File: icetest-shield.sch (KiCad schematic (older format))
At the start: 7 parts

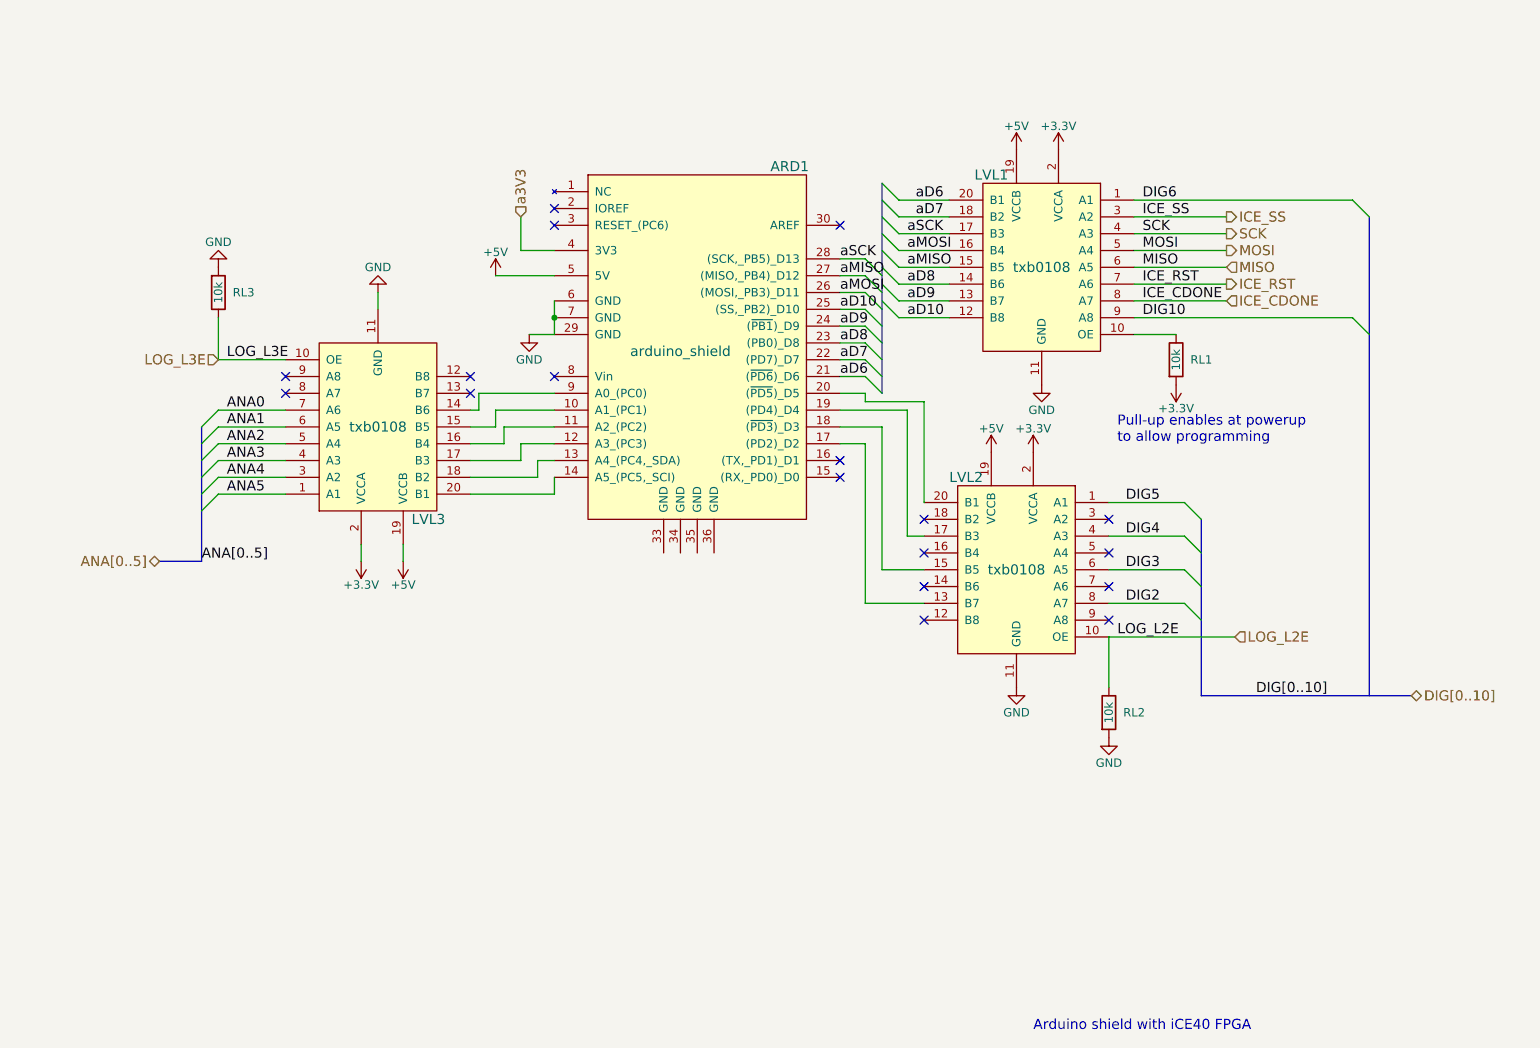
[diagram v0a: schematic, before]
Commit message: add SPI test points and verify footprints
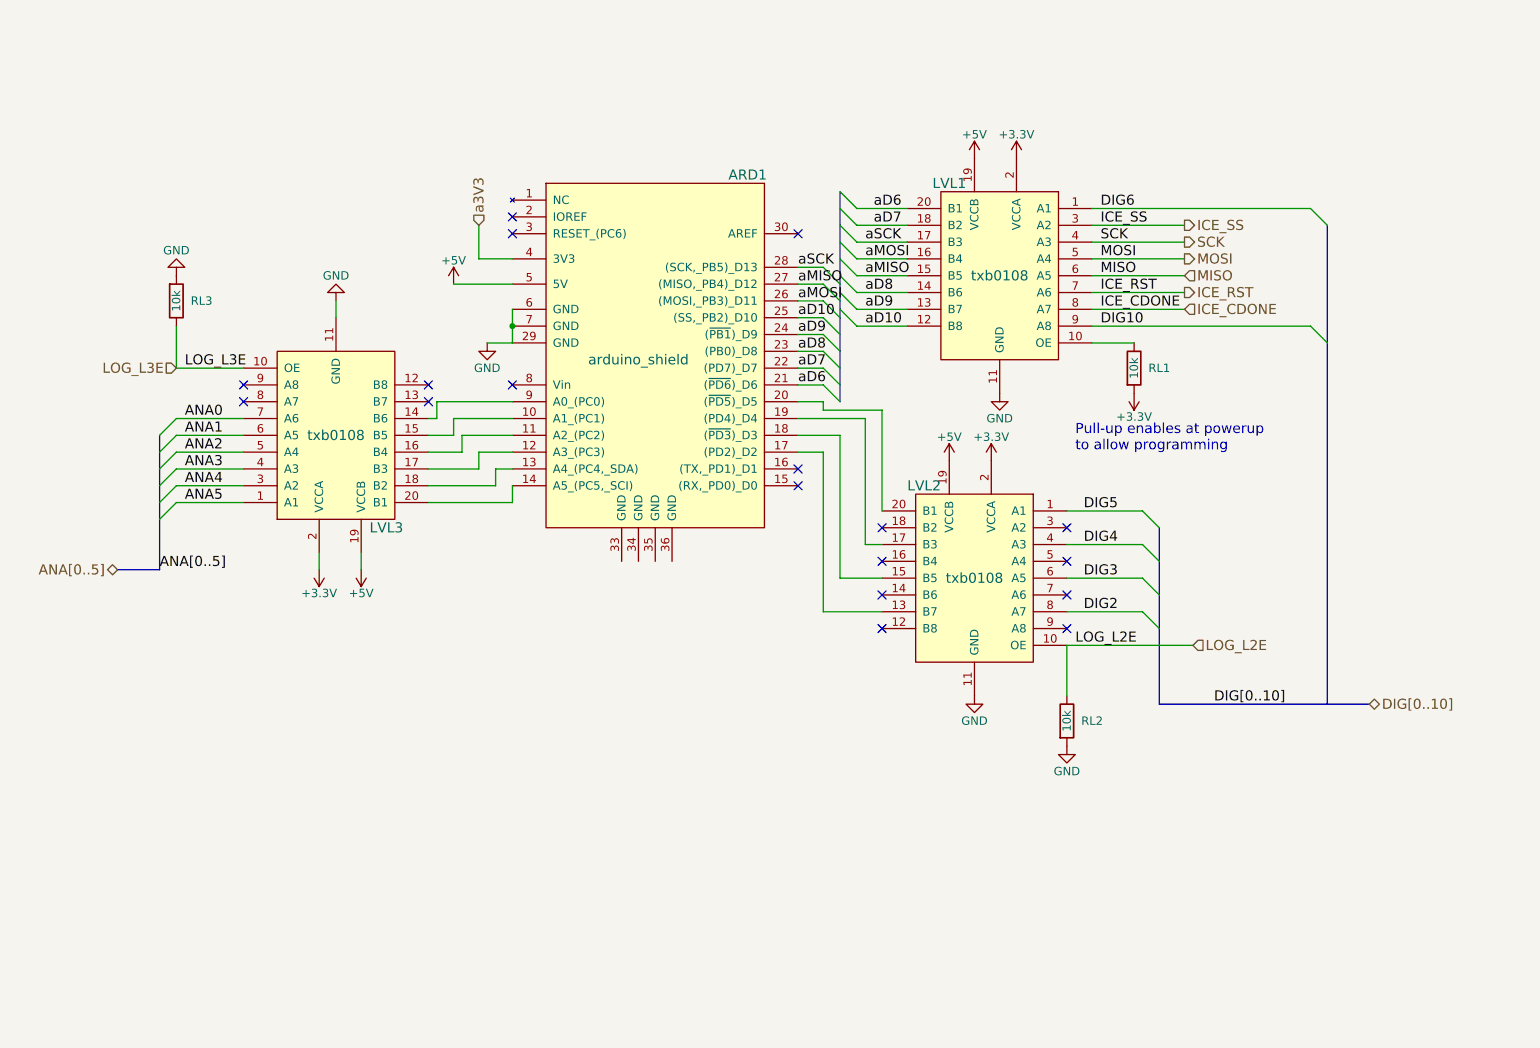
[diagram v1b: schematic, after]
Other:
- note removed: "Arduino shield with iCE40 FPGA"
- moved on the sheet: ARD1, LVL1, LVL2, LVL3, RL1, RL2, RL3

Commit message: route it
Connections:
- net GND: now also ARD1.33 (GND), ARD1.34 (GND), ARD1.35 (GND), ARD1.36 (GND)
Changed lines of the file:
@@
 	-1   0    0    1
 $EndComp
-Text HLabel 4050 2700 1    60   Input ~ 0
+Text HLabel 4050 2700 1    60   Output ~ 0
 a3V3
 NoConn ~ 5950 4150
@@
 Text HLabel 2250 3550 0    60   Input ~ 0
 LOG_L3E
+$Comp
+L GND #PWR?
+U 1 1 5793C5E6
+P 5100 4700
+F 0 "#PWR?" H 5100 4450 50  0001 C CNN
+F 1 "GND" H 5100 4550 50  0000 C CNN
+F 2 "" H 5100 4700 50  0000 C CNN
+F 3 "" H 5100 4700 50  0000 C CNN
+	1    5100 4700
+	-1   0    0    -1
+$EndComp
+Wire Wire Line
+	4900 4700 5200 4700
+Connection ~ 5100 4700
+Connection ~ 5000 4700
 $EndSCHEMATC

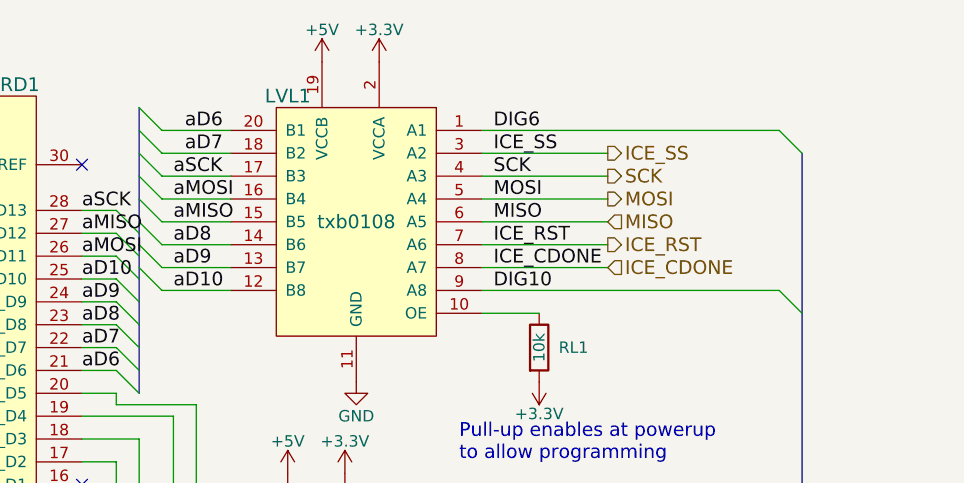
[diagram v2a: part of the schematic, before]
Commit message: fix ard symbol and route
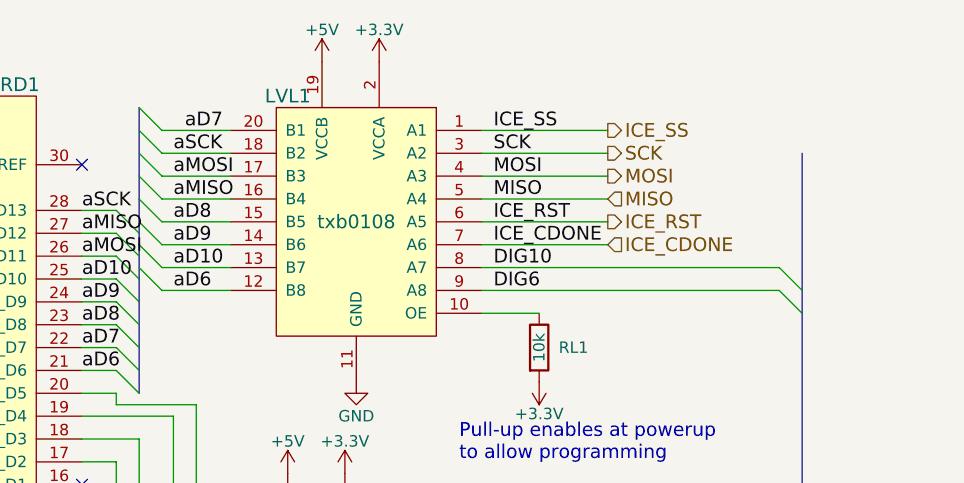
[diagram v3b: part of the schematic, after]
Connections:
- net DIG10: now also LVL1.8 (A7); no longer LVL1.9 (A8)
- net DIG6: now also LVL1.9 (A8); no longer LVL1.1 (A1)
- net ICE_CDONE: now also LVL1.7 (A6); no longer LVL1.8 (A7)
- net ICE_RST: now also LVL1.6 (A5); no longer LVL1.7 (A6)
- net ICE_SS: now also LVL1.1 (A1); no longer LVL1.3 (A2)
- net MISO: now also LVL1.5 (A4); no longer LVL1.6 (A5)
- net MOSI: now also LVL1.4 (A3); no longer LVL1.5 (A4)
- net SCK: now also LVL1.3 (A2); no longer LVL1.4 (A3)
- net aD10: now also LVL1.13 (B7); no longer LVL1.12 (B8)
- net aD6: now also LVL1.12 (B8); no longer LVL1.20 (B1)
- net aD7: now also LVL1.20 (B1); no longer LVL1.18 (B2)
- net aD8: now also LVL1.15 (B5); no longer LVL1.14 (B6)
- net aD9: now also LVL1.14 (B6); no longer LVL1.13 (B7)
- net aMISO: now also LVL1.16 (B4); no longer LVL1.15 (B5)
- net aMOSI: now also LVL1.17 (B3); no longer LVL1.16 (B4)
- net aSCK: now also LVL1.18 (B2); no longer LVL1.17 (B3)
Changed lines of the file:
@@
 $EndComp
+Entry Wire Line
+	6200 3200 6300 3300
+Entry Wire Line
+	6200 2600 6300 2700
+Entry Wire Line
+	6100 3650 6200 3750
 Entry Wire Line
 	6200 2500 6300 2600
@@
 	6200 2700 6300 2800
 Entry Wire Line
-	6100 3650 6200 3750
-Entry Wire Line
-	6200 2600 6300 2700
-Entry Wire Line
 	6200 2800 6300 2900
 Entry Wire Line
@@
 Entry Wire Line
 	6200 3100 6300 3200
-Entry Wire Line
-	6200 3200 6300 3300
 Entry Wire Line
 	6100 3550 6200 3650
@@
 Text Label 5950 3650 0    60   ~ 0
 aD6
+Text Label 6350 3300 0    60   ~ 0
+aD6
 Text Label 6400 2600 0    60   ~ 0
-aD6
-Text Label 6400 2700 0    60   ~ 0
 aD7
+Text Label 6350 2700 0    60   ~ 0
+aSCK
 Text Label 6350 2800 0    60   ~ 0
-aSCK
+aMOSI
 Text Label 6350 2900 0    60   ~ 0
-aMOSI
+aMISO
 Text Label 6350 3000 0    60   ~ 0
-aMISO
+aD8
 Text Label 6350 3100 0    60   ~ 0
-aD8
+aD9
 Text Label 6350 3200 0    60   ~ 0
-aD9
-Text Label 6350 3300 0    60   ~ 0
 aD10
 NoConn ~ 6450 4500
@@
 Text Notes 7600 4050 0    60   ~ 0
 Pull-up enables at powerup\nto allow programming
+Text Label 7750 3300 0    60   ~ 0
+DIG6
 Text Label 7750 2600 0    60   ~ 0
-DIG6
+ICE_SS
 Text Label 7750 2700 0    60   ~ 0
-ICE_SS
+SCK
 Text Label 7750 2800 0    60   ~ 0
-SCK
+MOSI
 Text Label 7750 2900 0    60   ~ 0
-MOSI
+MISO
 Text Label 7750 3000 0    60   ~ 0
-MISO
+ICE_RST
 Text Label 7750 3100 0    60   ~ 0
-ICE_RST
+ICE_CDONE
 Text Label 7750 3200 0    60   ~ 0
-ICE_CDONE
-Text Label 7750 3300 0    60   ~ 0
 DIG10
 Entry Wire Line
@@
 NoConn ~ 5950 4150
 NoConn ~ 5950 4250
+Text HLabel 8250 2700 2    60   Output ~ 0
+SCK
 Text HLabel 8250 2800 2    60   Output ~ 0
-SCK
-Text HLabel 8250 2900 2    60   Output ~ 0
 MOSI
-Text HLabel 8250 3000 2    60   Input ~ 0
+Text HLabel 8250 2900 2    60   Input ~ 0
 MISO
 Wire Wire Line
@@
 	3100 4650 3100 4750
 Wire Wire Line
-	6600 2600 6300 2600
+	6300 2600 6600 2600
 Wire Wire Line
 	6300 2700 6600 2700
@@
 	6300 3200 6600 3200
 Wire Wire Line
-	6300 3300 6600 3300
-Wire Wire Line
 	6100 2950 5950 2950
 Wire Wire Line
@@
 	6200 2500 6200 3750
 Wire Wire Line
-	7700 2600 9000 2600
-Wire Wire Line
-	8250 2700 7700 2700
-Wire Wire Line
-	7700 2800 8250 2800
-Wire Wire Line
-	8250 2900 7700 2900
+	8250 2600 7700 2600
+Wire Wire Line
+	7700 2700 8250 2700
+Wire Wire Line
+	8250 2800 7700 2800
+Wire Wire Line
+	7700 2900 8250 2900
 Wire Wire Line
 	7700 3000 8250 3000
 Wire Wire Line
-	7700 3100 8250 3100
-Wire Wire Line
-	8250 3200 7700 3200
-Wire Wire Line
-	7700 3300 9000 3300
+	8250 3100 7700 3100
 Wire Wire Line
 	7700 3400 7950 3400
@@
 Wire Wire Line
 	4050 2900 4050 2700
-Text HLabel 8250 2700 2    60   Output ~ 0
+Text HLabel 8250 2600 2    60   Output ~ 0
 ICE_SS
-Text HLabel 8250 3100 2    60   Output ~ 0
+Text HLabel 8250 3000 2    60   Output ~ 0
 ICE_RST
-Text HLabel 8250 3200 2    60   Input ~ 0
+Text HLabel 8250 3100 2    60   Input ~ 0
 ICE_CDONE
 Entry Wire Line
-	9000 2600 9100 2700
+	9000 3200 9100 3300
 Entry Wire Line
 	9000 3300 9100 3400
@@
 LOG_L3E
 $Comp
-L GND #PWR?
+L GND #PWR090
 U 1 1 5793C5E6
 P 5100 4700
-F 0 "#PWR?" H 5100 4450 50  0001 C CNN
+F 0 "#PWR090" H 5100 4450 50  0001 C CNN
 F 1 "GND" H 5100 4550 50  0000 C CNN
 F 2 "" H 5100 4700 50  0000 C CNN
@@
 Connection ~ 5100 4700
 Connection ~ 5000 4700
+Wire Wire Line
+	6600 3300 6300 3300
+Wire Wire Line
+	9000 3200 7700 3200
+Wire Wire Line
+	9000 3300 7700 3300
 $EndSCHEMATC

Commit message: fix schematic bugs
signal on N/C pin on ice40
1.2V regulator R divider moved to input side
Remove R divider for 3.3V (not needed for fixed V model)
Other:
- note added: "Pull-down holds tri-state\nuntil fpga outputs enabled"
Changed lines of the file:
@@
 $EndComp
 $Comp
-L GND #PWR076
+L GND #PWR077
 U 1 1 578B7F2F
 P 4100 3400
-F 0 "#PWR076" H 4100 3150 50  0001 C CNN
+F 0 "#PWR077" H 4100 3150 50  0001 C CNN
 F 1 "GND" H 4100 3250 50  0000 C CNN
 F 2 "" H 4100 3400 50  0000 C CNN
@@
 $EndComp
 $Comp
-L +5V #PWR077
+L +5V #PWR078
 U 1 1 578B7F35
 P 3900 3050
-F 0 "#PWR077" H 3900 2900 50  0001 C CNN
+F 0 "#PWR078" H 3900 2900 50  0001 C CNN
 F 1 "+5V" H 3900 3190 50  0000 C CNN
 F 2 "" H 3900 3050 50  0000 C CNN
@@
 NoConn ~ 5950 2750
 $Comp
-L GND #PWR078
+L GND #PWR079
 U 1 1 578B7F4E
 P 3200 3150
-F 0 "#PWR078" H 3200 2900 50  0001 C CNN
+F 0 "#PWR079" H 3200 2900 50  0001 C CNN
 F 1 "GND" H 3200 3000 50  0000 C CNN
 F 2 "" H 3200 3150 50  0000 C CNN
@@
 $EndComp
 $Comp
-L +5V #PWR079
+L +5V #PWR080
 U 1 1 578B7F54
 P 3350 4750
-F 0 "#PWR079" H 3350 4600 50  0001 C CNN
+F 0 "#PWR080" H 3350 4600 50  0001 C CNN
 F 1 "+5V" H 3350 4890 50  0000 C CNN
 F 2 "" H 3350 4750 50  0000 C CNN
@@
 $EndComp
 $Comp
-L +3.3V #PWR080
+L +3.3V #PWR081
 U 1 1 578B7F5A
 P 3100 4750
-F 0 "#PWR080" H 3100 4600 50  0001 C CNN
+F 0 "#PWR081" H 3100 4600 50  0001 C CNN
 F 1 "+3.3V" H 3100 4890 50  0000 C CNN
 F 2 "" H 3100 4750 50  0000 C CNN
@@
 $EndComp
 $Comp
-L +3.3V #PWR081
+L +3.3V #PWR082
 U 1 1 578B7F72
 P 7100 4100
-F 0 "#PWR081" H 7100 3950 50  0001 C CNN
+F 0 "#PWR082" H 7100 3950 50  0001 C CNN
 F 1 "+3.3V" H 7100 4240 50  0000 C CNN
 F 2 "" H 7100 4100 50  0000 C CNN
@@
 $EndComp
 $Comp
-L +5V #PWR082
+L +5V #PWR083
 U 1 1 578B7F78
 P 6850 4100
-F 0 "#PWR082" H 6850 3950 50  0001 C CNN
+F 0 "#PWR083" H 6850 3950 50  0001 C CNN
 F 1 "+5V" H 6850 4240 50  0000 C CNN
 F 2 "" H 6850 4100 50  0000 C CNN
@@
 $EndComp
 $Comp
-L GND #PWR083
+L GND #PWR084
 U 1 1 578B7F7E
 P 7150 3700
-F 0 "#PWR083" H 7150 3450 50  0001 C CNN
+F 0 "#PWR084" H 7150 3450 50  0001 C CNN
 F 1 "GND" H 7150 3550 50  0000 C CNN
 F 2 "" H 7150 3700 50  0000 C CNN
@@
 $EndComp
 $Comp
-L GND #PWR084
+L GND #PWR085
 U 1 1 578B7F84
 P 7000 5500
-F 0 "#PWR084" H 7000 5250 50  0001 C CNN
+F 0 "#PWR085" H 7000 5250 50  0001 C CNN
 F 1 "GND" H 7000 5350 50  0000 C CNN
 F 2 "" H 7000 5500 50  0000 C CNN
@@
 $EndComp
 $Comp
-L +3.3V #PWR085
+L +3.3V #PWR086
 U 1 1 578B7F8A
 P 7250 2300
-F 0 "#PWR085" H 7250 2150 50  0001 C CNN
+F 0 "#PWR086" H 7250 2150 50  0001 C CNN
 F 1 "+3.3V" H 7250 2440 50  0000 C CNN
 F 2 "" H 7250 2300 50  0000 C CNN
@@
 $EndComp
 $Comp
-L +5V #PWR086
+L +5V #PWR087
 U 1 1 578B7F90
 P 7000 2300
-F 0 "#PWR086" H 7000 2150 50  0001 C CNN
+F 0 "#PWR087" H 7000 2150 50  0001 C CNN
 F 1 "+5V" H 7000 2440 50  0000 C CNN
 F 2 "" H 7000 2300 50  0000 C CNN
@@
 $EndComp
 $Comp
-L +3.3V #PWR087
+L +3.3V #PWR088
 U 1 1 578B8844
 P 7950 3700
-F 0 "#PWR087" H 7950 3550 50  0001 C CNN
+F 0 "#PWR088" H 7950 3550 50  0001 C CNN
 F 1 "+3.3V" H 7950 3840 50  0000 C CNN
 F 2 "" H 7950 3700 50  0000 C CNN
@@
 $EndComp
 $Comp
-L GND #PWR088
+L GND #PWR089
 U 1 1 578B7AFA
 P 7550 5800
-F 0 "#PWR088" H 7550 5550 50  0001 C CNN
+F 0 "#PWR089" H 7550 5550 50  0001 C CNN
 F 1 "GND" H 7550 5650 50  0000 C CNN
 F 2 "" H 7550 5800 50  0000 C CNN
@@
 $EndComp
 $Comp
-L GND #PWR089
+L GND #PWR090
 U 1 1 578B7C6A
 P 2250 3000
-F 0 "#PWR089" H 2250 2750 50  0001 C CNN
+F 0 "#PWR090" H 2250 2750 50  0001 C CNN
 F 1 "GND" H 2250 2850 50  0000 C CNN
 F 2 "" H 2250 3000 50  0000 C CNN
@@
 Entry Wire Line
 	9000 3300 9100 3400
-Wire Bus Line
-	9100 5550 9100 2700
 Text HLabel 9350 5550 2    60   BiDi ~ 0
 DIG[0..10]
@@
 LOG_L3E
 $Comp
-L GND #PWR090
+L GND #PWR091
 U 1 1 5793C5E6
 P 5100 4700
-F 0 "#PWR090" H 5100 4450 50  0001 C CNN
+F 0 "#PWR091" H 5100 4450 50  0001 C CNN
 F 1 "GND" H 5100 4550 50  0000 C CNN
 F 2 "" H 5100 4700 50  0000 C CNN
@@
 Wire Wire Line
 	9000 3300 7700 3300
+Text Notes 7100 6200 0    60   ~ 0
+Pull-down holds tri-state\nuntil fpga outputs enabled
+Wire Bus Line
+	9100 3300 9100 5550
 $EndSCHEMATC
